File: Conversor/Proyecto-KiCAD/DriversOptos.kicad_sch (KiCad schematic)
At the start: 22 parts, among them U1 ACPL-P480, U2 ACPL-P480, U3 ACPL-P480, U4 ACPL-P480, U5 2ED21834-S06J, U6 2ED21834-S06J

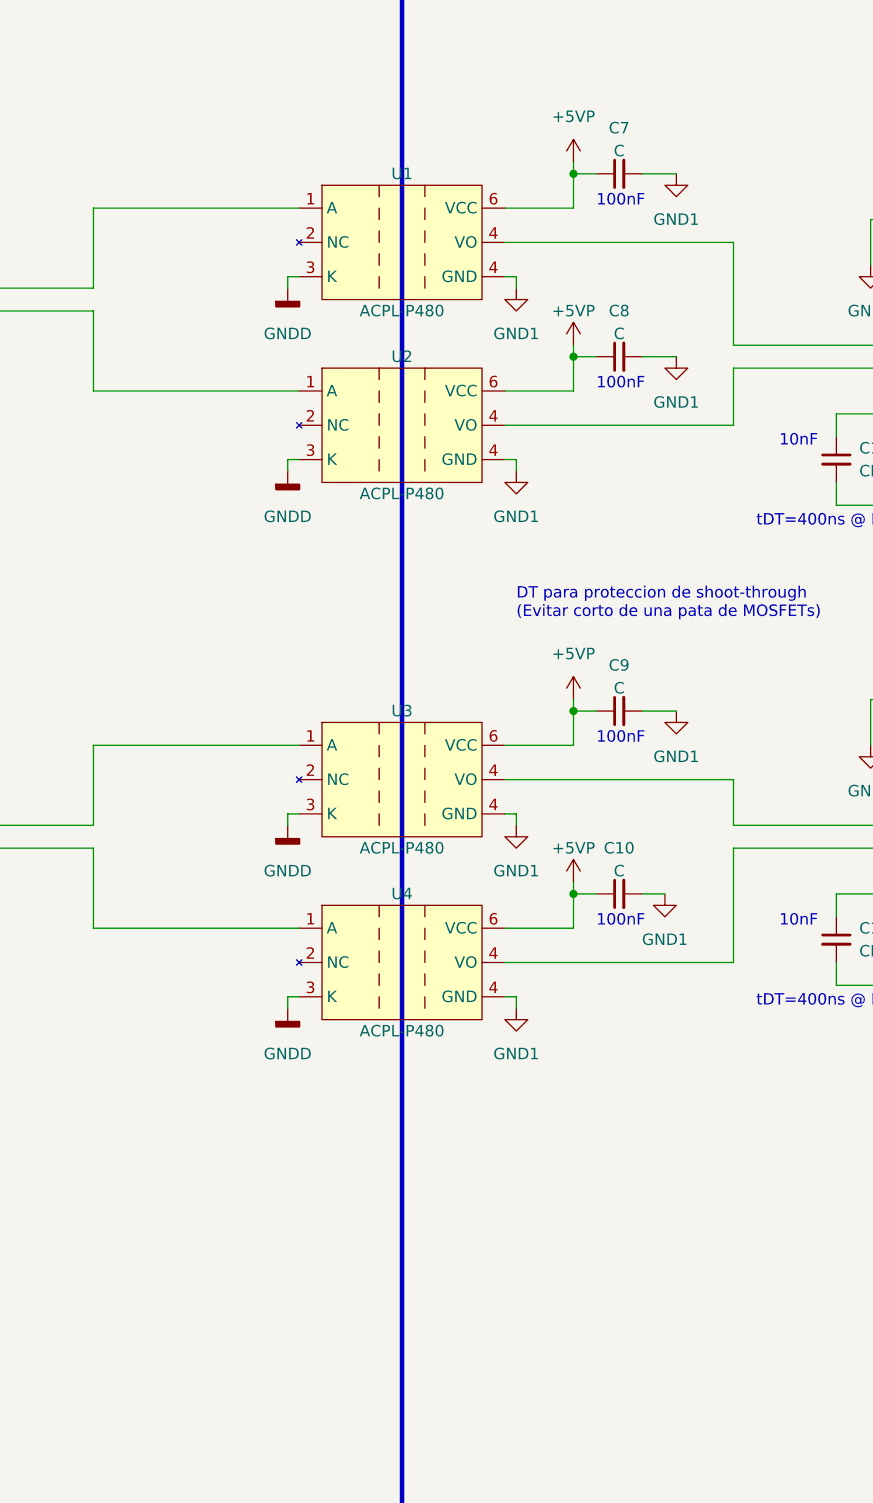
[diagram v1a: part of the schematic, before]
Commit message: Seleccionar componentes de los que me dieron y seguir con la placa adaptadora
- OpAmp OPA365AID para acondicionamiento de señales del sensor de efecto
hall
- Los optos que hay son ACPL-P343 en vez de P480, que necesitan 15-30V
de alimentación. Preguntar si no es mejor cambiarlos por 6N137, de 5V de
Vcc
- Regulador solo hay LM7805 de 5Vout pero también necesito 3.3Vout
- No hay ningún diodo en las cosas que me dieron

Por hacer:
  - Preguntar por los 6N137 y algun regulador de 3V3 out
  - Preguntar por los diodos del puente del conversor
  - Terminar de pasar la placa adaptadora del DSP
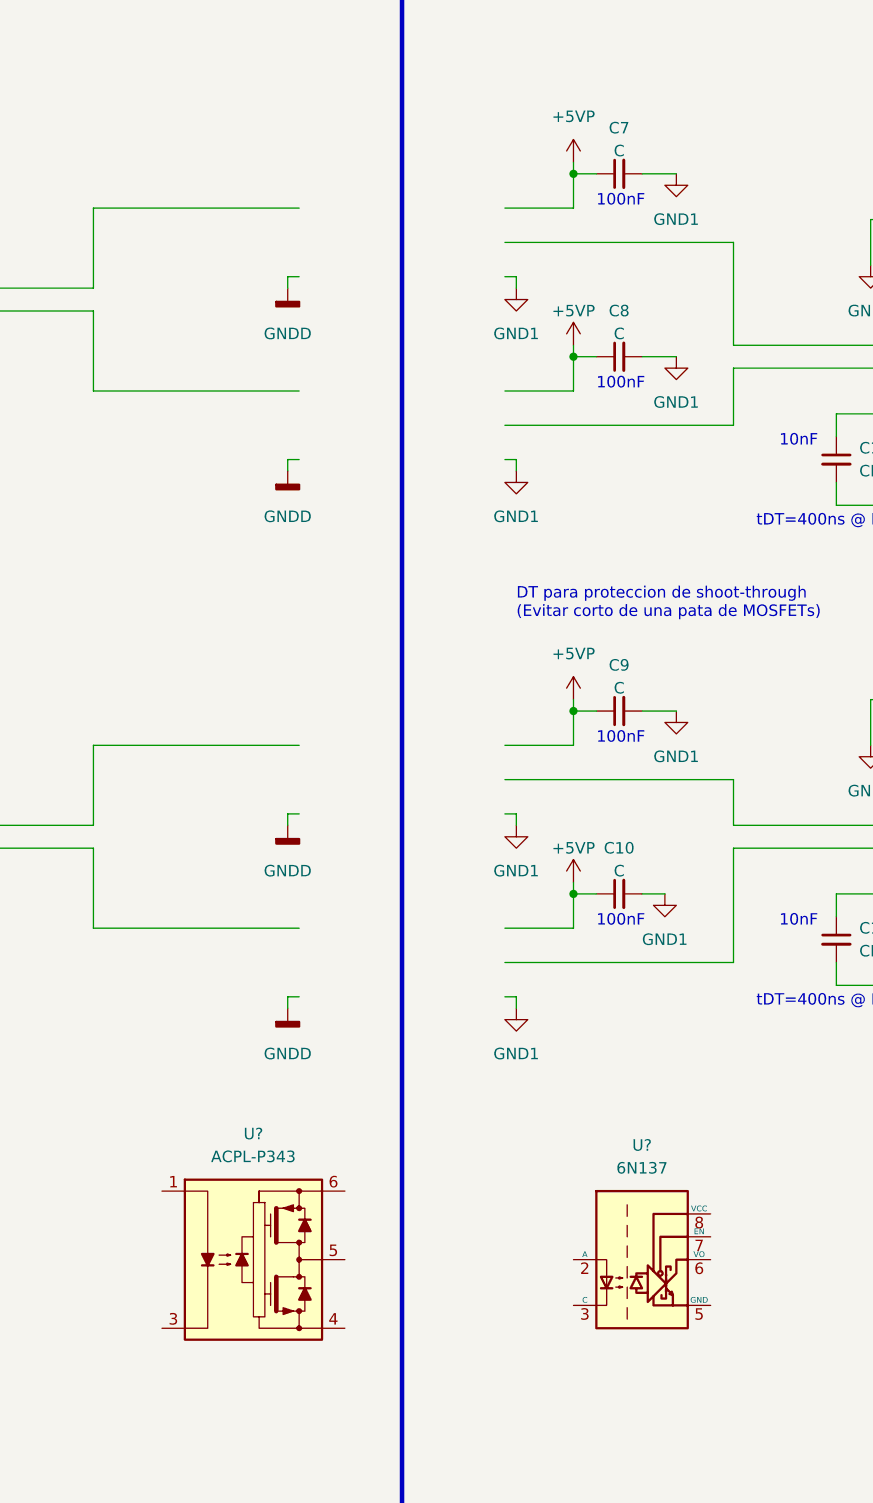
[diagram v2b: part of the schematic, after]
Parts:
- removed U1, U2, U3, U4: ACPL-P480, Package_SO:SSO-6_6.8x4.6mm_P1.27mm_Clearance7mm, symbol Componentes proyecto:ACPL-P480
- added U?: 6N137, Package_DIP:DIP-8_W7.62mm, symbol Isolator:6N137
- added U?: ACPL-P343, Package_SO:SSO-6_6.8x4.6mm_P1.27mm_Clearance7mm, symbol Driver_FET:ACPL-P343
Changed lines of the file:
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@@
     (pin "1")
-  )
-  (symbol (lib_id "Componentes proyecto:ACPL-P480") (at 125.73 54.61 0) (unit 1)
-    (in_bom yes) (on_board yes)
-    (property "Reference" "U1" (id 0) (at 125.73 46.99 0))
-    (property "Value" "ACPL-P480" (id 1) (at 125.73 62.23 0))
-    (property "Footprint" "Package_SO:SSO-6_6.8x4.6mm_P1.27mm_Clearance7mm" (id 2) (at 125.73 54.61 0)
-      (effects (font (size 1.27 1.27)) hide)
-    )
-    (property "Datasheet" "" (id 3) (at 125.73 54.61 0)
-      (effects (font (size 1.27 1.27)) hide)
-    )
-    (pin "1")
-    (pin "2")
-    (pin "3")
-    (pin "4")
-    (pin "4")
-    (pin "6")
   )
   (symbol (lib_id "power:GND1") (at 156.21 106.68 0) (unit 1)
@@
     )
     (pin "1")
+  )
+  (symbol (lib_id "Isolator:6N137") (at 152.4 167.64 0) (unit 1)
+    (in_bom yes) (on_board yes) (fields_autoplaced)
+    (property "Reference" "U?" (id 0) (at 152.4 154.94 0))
+    (property "Value" "6N137" (id 1) (at 152.4 157.48 0))
+    (property "Footprint" "Package_DIP:DIP-8_W7.62mm" (id 2) (at 152.4 180.34 0)
+      (effects (font (size 1.27 1.27)) hide)
+    )
+    (property "Datasheet" "https://docs.broadcom.com/docs/AV02-0940EN" (id 3) (at 130.81 153.67 0)
+      (effects (font (size 1.27 1.27)) hide)
+    )
+    (pin "1")
+    (pin "2")
+    (pin "3")
+    (pin "5")
+    (pin "6")
+    (pin "7")
+    (pin "8")
   )
   (symbol (lib_id "Device:R_US") (at 212.09 116.84 90) (unit 1)
@@
     (pin "1")
   )
-  (symbol (lib_name "ACPL-P480_1") (lib_id "Componentes proyecto:ACPL-P480") (at 125.73 134.62 0) (unit 1)
-    (in_bom yes) (on_board yes)
-    (property "Reference" "U4" (id 0) (at 125.73 127 0))
-    (property "Value" "ACPL-P480" (id 1) (at 125.73 142.24 0))
-    (property "Footprint" "Package_SO:SSO-6_6.8x4.6mm_P1.27mm_Clearance7mm" (id 2) (at 125.73 134.62 0)
-      (effects (font (size 1.27 1.27)) hide)
-    )
-    (property "Datasheet" "" (id 3) (at 125.73 134.62 0)
-      (effects (font (size 1.27 1.27)) hide)
-    )
-    (pin "1")
-    (pin "2")
-    (pin "3")
-    (pin "4")
-    (pin "4")
-    (pin "6")
-  )
   (symbol (lib_id "power:GNDD") (at 113.03 119.38 0) (unit 1)
     (in_bom yes) (on_board yes) (fields_autoplaced)
@@
     (pin "1")
   )
+  (symbol (lib_id "Driver_FET:ACPL-P343") (at 109.22 167.64 0) (unit 1)
+    (in_bom yes) (on_board yes) (fields_autoplaced)
+    (property "Reference" "U?" (id 0) (at 109.22 153.67 0))
+    (property "Value" "ACPL-P343" (id 1) (at 109.22 156.21 0))
+    (property "Footprint" "Package_SO:SSO-6_6.8x4.6mm_P1.27mm_Clearance7mm" (id 2) (at 109.22 177.8 0)
+      (effects (font (size 1.27 1.27) italic) hide)
+    )
+    (property "Datasheet" "https://docs.broadcom.com/docs/AV02-2928EN" (id 3) (at 106.934 167.513 0)
+      (effects (font (size 1.27 1.27)) (justify left) hide)
+    )
+    (pin "1")
+    (pin "2")
+    (pin "3")
+    (pin "4")
+    (pin "5")
+    (pin "6")
+  )
   (symbol (lib_id "Device:C_Small") (at 184.15 52.07 90) (unit 1)
     (in_bom yes) (on_board yes) (fields_autoplaced)
@@
     (pin "1")
   )
-  (symbol (lib_name "ACPL-P480_3") (lib_id "Componentes proyecto:ACPL-P480") (at 125.73 74.93 0) (unit 1)
-    (in_bom yes) (on_board yes)
-    (property "Reference" "U2" (id 0) (at 125.73 67.31 0))
-    (property "Value" "ACPL-P480" (id 1) (at 125.73 82.55 0))
-    (property "Footprint" "Package_SO:SSO-6_6.8x4.6mm_P1.27mm_Clearance7mm" (id 2) (at 125.73 74.93 0)
-      (effects (font (size 1.27 1.27)) hide)
-    )
-    (property "Datasheet" "" (id 3) (at 125.73 74.93 0)
-      (effects (font (size 1.27 1.27)) hide)
-    )
-    (pin "1")
-    (pin "2")
-    (pin "3")
-    (pin "4")
-    (pin "4")
-    (pin "6")
-  )
-  (symbol (lib_name "ACPL-P480_2") (lib_id "Componentes proyecto:ACPL-P480") (at 125.73 114.3 0) (unit 1)
-    (in_bom yes) (on_board yes)
-    (property "Reference" "U3" (id 0) (at 125.73 106.68 0))
-    (property "Value" "ACPL-P480" (id 1) (at 125.73 121.92 0))
-    (property "Footprint" "Package_SO:SSO-6_6.8x4.6mm_P1.27mm_Clearance7mm" (id 2) (at 125.73 114.3 0)
-      (effects (font (size 1.27 1.27)) hide)
-    )
-    (property "Datasheet" "" (id 3) (at 125.73 114.3 0)
-      (effects (font (size 1.27 1.27)) hide)
-    )
-    (pin "1")
-    (pin "2")
-    (pin "3")
-    (pin "4")
-    (pin "4")
-    (pin "6")
-  )
   (symbol (lib_id "power:GND1") (at 156.21 67.31 0) (unit 1)

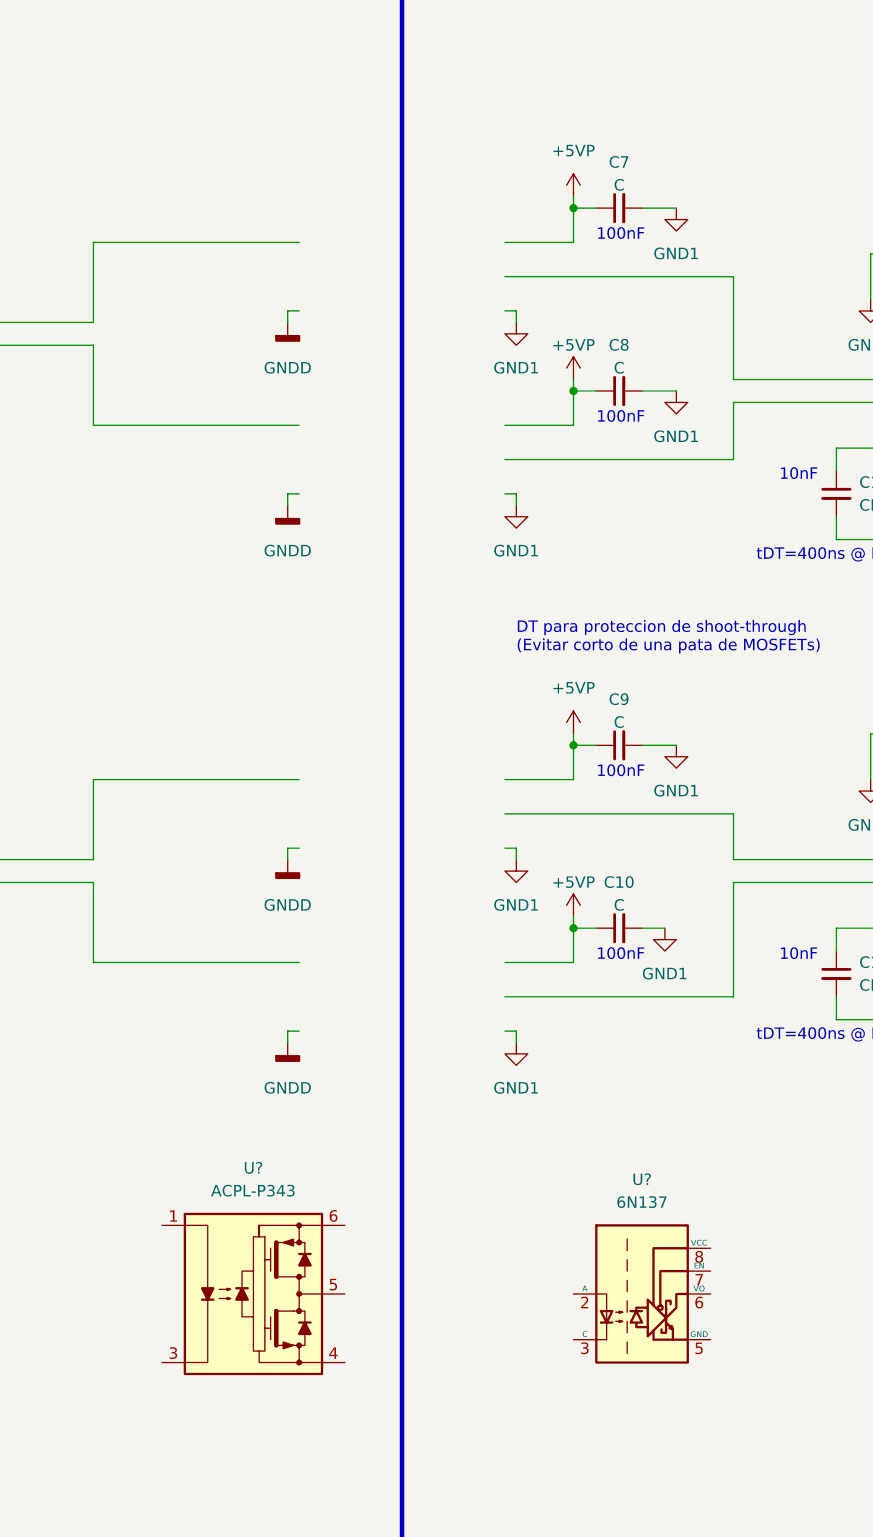
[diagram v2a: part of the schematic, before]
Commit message: Continuar el paso de la placa adaptadora al proyecto
- El bloque de encoder y DAC se eliminan, no son necesarios
- Hay que agregar un selector entre 5V externo y por USB para el DSP, y ver como compatibilizarlo con la alimentación general
- Para el regulador de 3.3V se usa el mismo integrado que en la placa adaptadora (TI LP2985-3.3)
- Los optos son los ACPL-P480 en vez de los P343
Por hacer:
  - Terminar la placa adaptadora (USB-UART, Power Supply e I2C)
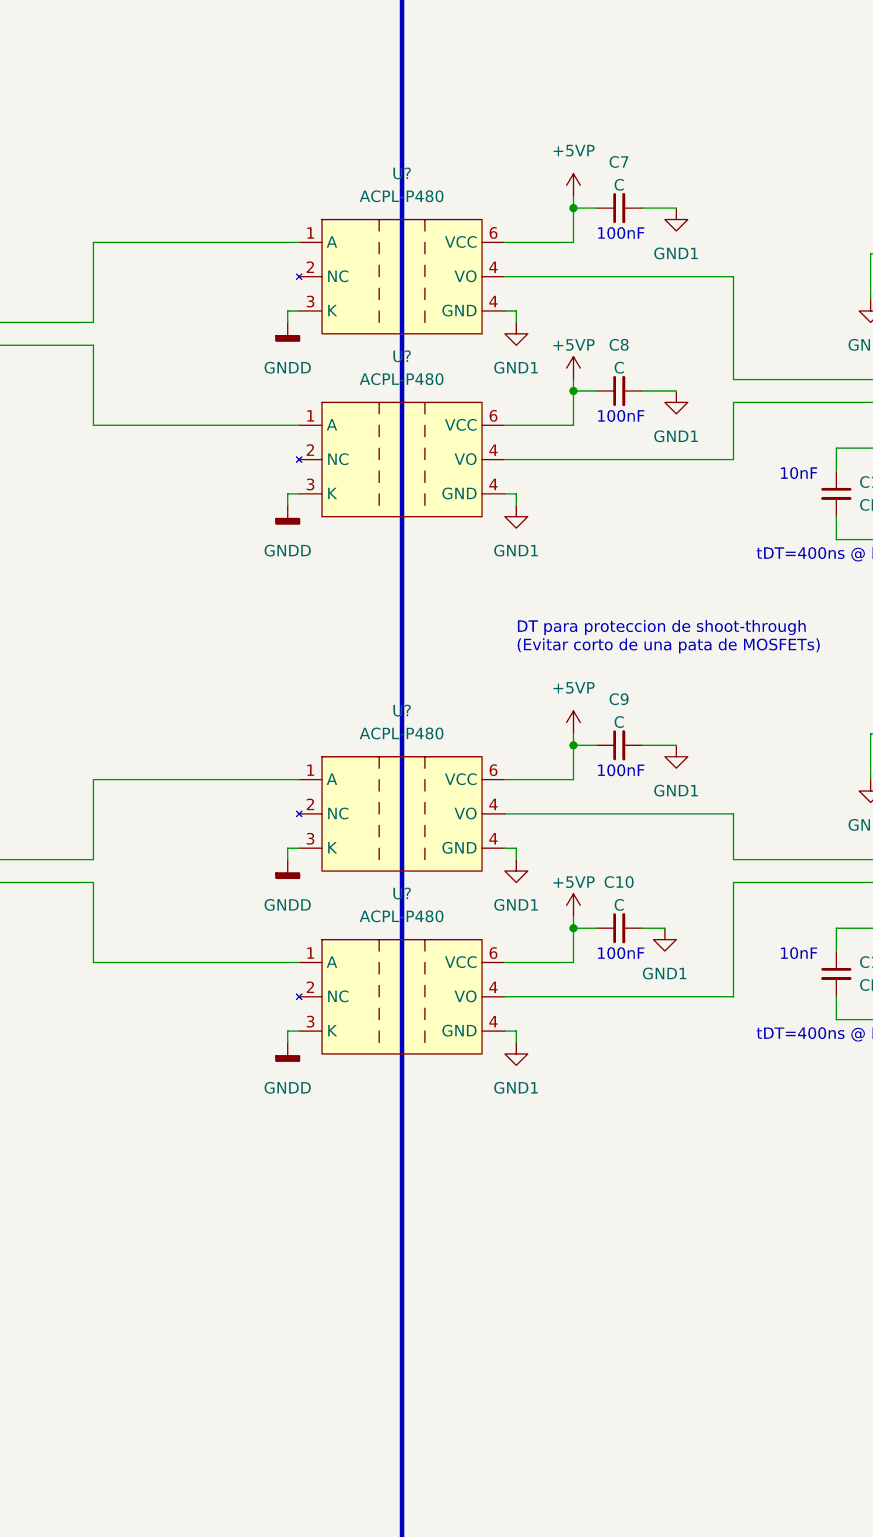
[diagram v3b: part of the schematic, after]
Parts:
- removed U?: 6N137, Package_DIP:DIP-8_W7.62mm, symbol Isolator:6N137
- removed U?: ACPL-P343, Package_SO:SSO-6_6.8x4.6mm_P1.27mm_Clearance7mm, symbol Driver_FET:ACPL-P343
- added U? (x4): ACPL-P480, symbol Componentes proyecto:ACPL-P480
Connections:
- net +5VP: now also U?.6 (VCC), U?.6 (VCC), U?.6 (VCC), U?.6 (VCC)
- net GND1: now also U?.4 (VO), U?.4 (VO), U?.4 (VO), U?.4 (VO)
- net GNDD: now also U?.3 (K), U?.3 (K), U?.3 (K), U?.3 (K)
- net PWM1: now also U?.1 (A)
- net PWM2: now also U?.1 (A)
- net /PWM3: now also U?.1 (A)
- net /PWM4: now also U?.1 (A)
- net at U6.1 (HIN): now also U?.4 (VO)
- net at U6.2 (/LIN): now also U?.4 (VO)
- net at U5.1 (HIN): now also U?.4 (VO)
- net at U5.2 (/LIN): now also U?.4 (VO)
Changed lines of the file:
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@@
     (pin "2")
+  )
+  (symbol (lib_id "Componentes proyecto:ACPL-P480") (at 125.73 54.61 0) (unit 1)
+    (in_bom yes) (on_board yes) (fields_autoplaced)
+    (property "Reference" "U?" (id 0) (at 125.73 43.18 0))
+    (property "Value" "ACPL-P480" (id 1) (at 125.73 45.72 0))
+    (property "Footprint" "" (id 2) (at 125.73 54.61 0)
+      (effects (font (size 1.27 1.27)) hide)
+    )
+    (property "Datasheet" "" (id 3) (at 125.73 54.61 0)
+      (effects (font (size 1.27 1.27)) hide)
+    )
+    (pin "1")
+    (pin "2")
+    (pin "3")
+    (pin "4")
+    (pin "4")
+    (pin "6")
   )
   (symbol (lib_id "Device:C_Small") (at 204.47 120.65 0) (unit 1)
@@
     (pin "2")
   )
+  (symbol (lib_id "Componentes proyecto:ACPL-P480") (at 125.73 134.62 0) (unit 1)
+    (in_bom yes) (on_board yes) (fields_autoplaced)
+    (property "Reference" "U?" (id 0) (at 125.73 123.19 0))
+    (property "Value" "ACPL-P480" (id 1) (at 125.73 125.73 0))
+    (property "Footprint" "" (id 2) (at 125.73 134.62 0)
+      (effects (font (size 1.27 1.27)) hide)
+    )
+    (property "Datasheet" "" (id 3) (at 125.73 134.62 0)
+      (effects (font (size 1.27 1.27)) hide)
+    )
+    (pin "1")
+    (pin "2")
+    (pin "3")
+    (pin "4")
+    (pin "4")
+    (pin "6")
+  )
   (symbol (lib_id "power:+5VP") (at 144.78 45.72 0) (unit 1)
     (in_bom yes) (on_board yes) (fields_autoplaced)
@@
     )
     (pin "1")
-  )
-  (symbol (lib_id "Isolator:6N137") (at 152.4 167.64 0) (unit 1)
-    (in_bom yes) (on_board yes) (fields_autoplaced)
-    (property "Reference" "U?" (id 0) (at 152.4 154.94 0))
-    (property "Value" "6N137" (id 1) (at 152.4 157.48 0))
-    (property "Footprint" "Package_DIP:DIP-8_W7.62mm" (id 2) (at 152.4 180.34 0)
-      (effects (font (size 1.27 1.27)) hide)
-    )
-    (property "Datasheet" "https://docs.broadcom.com/docs/AV02-0940EN" (id 3) (at 130.81 153.67 0)
-      (effects (font (size 1.27 1.27)) hide)
-    )
-    (pin "1")
-    (pin "2")
-    (pin "3")
-    (pin "5")
-    (pin "6")
-    (pin "7")
-    (pin "8")
   )
   (symbol (lib_id "Device:R_US") (at 212.09 116.84 90) (unit 1)
@@
     (pin "1")
   )
+  (symbol (lib_id "Componentes proyecto:ACPL-P480") (at 125.73 74.93 0) (unit 1)
+    (in_bom yes) (on_board yes) (fields_autoplaced)
+    (property "Reference" "U?" (id 0) (at 125.73 63.5 0))
+    (property "Value" "ACPL-P480" (id 1) (at 125.73 66.04 0))
+    (property "Footprint" "" (id 2) (at 125.73 74.93 0)
+      (effects (font (size 1.27 1.27)) hide)
+    )
+    (property "Datasheet" "" (id 3) (at 125.73 74.93 0)
+      (effects (font (size 1.27 1.27)) hide)
+    )
+    (pin "1")
+    (pin "2")
+    (pin "3")
+    (pin "4")
+    (pin "4")
+    (pin "6")
+  )
   (symbol (lib_id "power:GNDD") (at 113.03 119.38 0) (unit 1)
     (in_bom yes) (on_board yes) (fields_autoplaced)
@@
     )
     (pin "1")
-  )
-  (symbol (lib_id "Driver_FET:ACPL-P343") (at 109.22 167.64 0) (unit 1)
-    (in_bom yes) (on_board yes) (fields_autoplaced)
-    (property "Reference" "U?" (id 0) (at 109.22 153.67 0))
-    (property "Value" "ACPL-P343" (id 1) (at 109.22 156.21 0))
-    (property "Footprint" "Package_SO:SSO-6_6.8x4.6mm_P1.27mm_Clearance7mm" (id 2) (at 109.22 177.8 0)
-      (effects (font (size 1.27 1.27) italic) hide)
-    )
-    (property "Datasheet" "https://docs.broadcom.com/docs/AV02-2928EN" (id 3) (at 106.934 167.513 0)
-      (effects (font (size 1.27 1.27)) (justify left) hide)
-    )
-    (pin "1")
-    (pin "2")
-    (pin "3")
-    (pin "4")
-    (pin "5")
-    (pin "6")
   )
   (symbol (lib_id "Device:C_Small") (at 184.15 52.07 90) (unit 1)
@@
     (pin "1")
   )
+  (symbol (lib_id "Componentes proyecto:ACPL-P480") (at 125.73 114.3 0) (unit 1)
+    (in_bom yes) (on_board yes) (fields_autoplaced)
+    (property "Reference" "U?" (id 0) (at 125.73 102.87 0))
+    (property "Value" "ACPL-P480" (id 1) (at 125.73 105.41 0))
+    (property "Footprint" "" (id 2) (at 125.73 114.3 0)
+      (effects (font (size 1.27 1.27)) hide)
+    )
+    (property "Datasheet" "" (id 3) (at 125.73 114.3 0)
+      (effects (font (size 1.27 1.27)) hide)
+    )
+    (pin "1")
+    (pin "2")
+    (pin "3")
+    (pin "4")
+    (pin "4")
+    (pin "6")
+  )
   (symbol (lib_id "power:GND1") (at 156.21 46.99 0) (unit 1)
